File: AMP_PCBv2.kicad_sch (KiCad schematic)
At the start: 115 parts, among them J1 POWER, J2 EBRAKE, J3 MC, J4 STEERING, J5 OLED Breakout, J6 EBRAKE_BREAKOUT, Q1 Q_NMOS_GDS, Q2 Q_NMOS_GDS, Q3 Q_NMOS_GDS, Q4 Q_NMOS_GDS, U1 Teensy4.0, U10 RFM9x, U2 FT234XD, U3 LM1117-ADJ, U4 LM1117-ADJ, U5 74HC157, U6 74HC157, U7 74HC4060, U8 74HC00, U9 TLV272

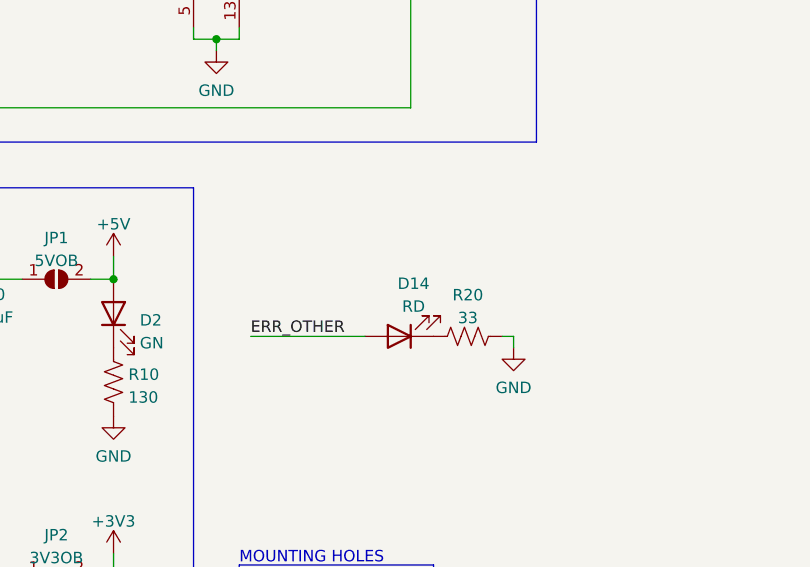
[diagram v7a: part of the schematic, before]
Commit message: Schematic clean up
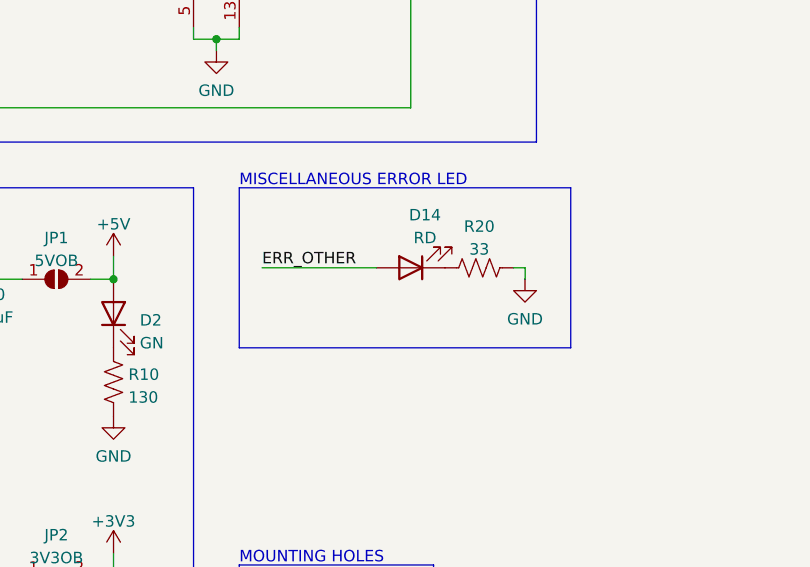
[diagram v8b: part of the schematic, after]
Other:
- note added: "MISCELLANEOUS ERROR LED"
- moved on the sheet: D14, R20
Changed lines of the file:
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@@
+    (stroke (width 0) (type default) (color 0 0 0 0))
+  )
+  (polyline (pts (xy 111.76 205.74) (xy 148.59 205.74))
     (stroke (width 0) (type default) (color 0 0 0 0))
   )
@@
     (stroke (width 0) (type default) (color 0 0 0 0))
   )
-  (wire (pts (xy 142.24 204.47) (xy 140.97 204.47))
+  (wire (pts (xy 143.51 196.85) (xy 142.24 196.85))
     (stroke (width 0) (type default) (color 0 0 0 0))
   )
@@
     (stroke (width 0) (type default) (color 0 0 0 0))
   )
+  (polyline (pts (xy 111.76 187.96) (xy 111.76 205.74))
+    (stroke (width 0) (type default) (color 0 0 0 0))
+  )
   (polyline (pts (xy 292.1 67.31) (xy 121.92 67.31))
     (stroke (width 0) (type default) (color 0 0 0 0))
@@
     (stroke (width 0) (type default) (color 0 0 0 0))
   )
+  (polyline (pts (xy 148.59 205.74) (xy 148.59 187.96))
+    (stroke (width 0) (type default) (color 0 0 0 0))
+  )
   (wire (pts (xy 261.62 212.09) (xy 261.62 214.63))
     (stroke (width 0) (type default) (color 0 0 0 0))
@@
     (stroke (width 0) (type default) (color 0 0 0 0))
   )
-  (wire (pts (xy 113.03 204.47) (xy 125.73 204.47))
+  (wire (pts (xy 114.3 196.85) (xy 127 196.85))
     (stroke (width 0) (type default) (color 0 0 0 0))
   )
@@
     (stroke (width 0) (type default) (color 0 0 0 0))
   )
-  (wire (pts (xy 142.24 205.74) (xy 142.24 204.47))
+  (wire (pts (xy 143.51 198.12) (xy 143.51 196.85))
     (stroke (width 0) (type default) (color 0 0 0 0))
   )
@@
     (stroke (width 0) (type default) (color 0 0 0 0))
   )
+  (polyline (pts (xy 148.59 187.96) (xy 111.76 187.96))
+    (stroke (width 0) (type default) (color 0 0 0 0))
+  )
   (wire (pts (xy 294.64 139.7) (xy 307.34 139.7))
     (stroke (width 0) (type default) (color 0 0 0 0))
@@
   )
   (text "EBRAKE BREAKOUT" (at 344.17 99.06 0)
+    (effects (font (size 1.27 1.27)) (justify left bottom))
+  )
+  (text "MISCELLANEOUS ERROR LED" (at 111.76 187.96 0)
     (effects (font (size 1.27 1.27)) (justify left bottom))
   )
@@
     (effects (font (size 1.27 1.27)) (justify right bottom))
   )
-  (label "ERR_OTHER" (at 113.03 204.47 0)
+  (label "ERR_OTHER" (at 114.3 196.85 0)
     (effects (font (size 1.27 1.27)) (justify left bottom))
   )
@@
     (pin "9")
   )
-  (symbol (lib_name "GND_2") (lib_id "power:GND") (at 142.24 205.74 0) (unit 1)
-    (in_bom yes) (on_board yes) (fields_autoplaced)
-    (property "Reference" "#PWR016" (id 0) (at 142.24 212.09 0)
-      (effects (font (size 1.27 1.27)) hide)
-    )
-    (property "Value" "GND" (id 1) (at 142.24 210.1834 0))
-    (property "Footprint" "" (id 2) (at 142.24 205.74 0)
-      (effects (font (size 1.27 1.27)) hide)
-    )
-    (property "Datasheet" "" (id 3) (at 142.24 205.74 0)
+  (symbol (lib_name "GND_2") (lib_id "power:GND") (at 143.51 198.12 0) (unit 1)
+    (in_bom yes) (on_board yes) (fields_autoplaced)
+    (property "Reference" "#PWR016" (id 0) (at 143.51 204.47 0)
+      (effects (font (size 1.27 1.27)) hide)
+    )
+    (property "Value" "GND" (id 1) (at 143.51 202.5634 0))
+    (property "Footprint" "" (id 2) (at 143.51 198.12 0)
+      (effects (font (size 1.27 1.27)) hide)
+    )
+    (property "Datasheet" "" (id 3) (at 143.51 198.12 0)
       (effects (font (size 1.27 1.27)) hide)
     )
@@
     (pin "1")
   )
-  (symbol (lib_id "Device:LED") (at 129.54 204.47 180) (unit 1)
-    (in_bom yes) (on_board yes) (fields_autoplaced)
-    (property "Reference" "D14" (id 0) (at 131.1275 198.6112 0))
-    (property "Value" "RD" (id 1) (at 131.1275 201.1481 0))
-    (property "Footprint" "LED_THT:LED_D5.0mm" (id 2) (at 129.54 204.47 0)
-      (effects (font (size 1.27 1.27)) hide)
-    )
-    (property "Datasheet" "~" (id 3) (at 129.54 204.47 0)
+  (symbol (lib_id "Device:LED") (at 130.81 196.85 180) (unit 1)
+    (in_bom yes) (on_board yes) (fields_autoplaced)
+    (property "Reference" "D14" (id 0) (at 132.3975 190.9912 0))
+    (property "Value" "RD" (id 1) (at 132.3975 193.5281 0))
+    (property "Footprint" "LED_THT:LED_D5.0mm" (id 2) (at 130.81 196.85 0)
+      (effects (font (size 1.27 1.27)) hide)
+    )
+    (property "Datasheet" "~" (id 3) (at 130.81 196.85 0)
       (effects (font (size 1.27 1.27)) hide)
     )
@@
     (pin "2")
   )
-  (symbol (lib_id "Device:R_US") (at 137.16 204.47 90) (unit 1)
-    (in_bom yes) (on_board yes) (fields_autoplaced)
-    (property "Reference" "R20" (id 0) (at 137.16 199.8812 90))
-    (property "Value" "33" (id 1) (at 137.16 202.4181 90))
-    (property "Footprint" "Resistor_SMD:R_0805_2012Metric_Pad1.20x1.40mm_HandSolder" (id 2) (at 137.414 203.454 90)
-      (effects (font (size 1.27 1.27)) hide)
-    )
-    (property "Datasheet" "~" (id 3) (at 137.16 204.47 0)
-      (effects (font (size 1.27 1.27)) hide)
-    )
+  (symbol (lib_id "Device:R_US") (at 138.43 196.85 90) (unit 1)
+    (in_bom yes) (on_board yes) (fields_autoplaced)
+    (property "Reference" "R20" (id 0) (at 138.43 192.2612 90))
+    (property "Value" "33" (id 1) (at 138.43 194.7981 90))
+    (property "Footprint" "Resistor_SMD:R_0805_2012Metric_Pad1.20x1.40mm_HandSolder" (id 2) (at 138.684 195.834 90)
+      (effects (font (size 1.27 1.27)) hide)
+    )
+    (property "Datasheet" "~" (id 3) (at 138.43 196.85 0)
+      (effects (font (size 1.27 1.27)) hide)
+    )
